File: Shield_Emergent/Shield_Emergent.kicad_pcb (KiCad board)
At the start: 2 copper layers, 33.4 x 63.5 mm, 23 parts, among them J1 Conn_01x02_Female, J2 Conn_01x04_Male, J3 Conn_01x02_Female, J4 Conn_01x04_Male, U1 Raspberri_Pi_Pico, U2 TPS2553, U3 TPS2553

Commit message: v1.3 Power of RPI_PICO and Shield was splitted
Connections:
- U1 pad 39: VBUS -> unconnected-(U1-Pad39)
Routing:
- net VBUS: track 36.0 -> 24.4 mm
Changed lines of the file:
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@@
   (net 36 "unconnected-(U1-Pad40)")
   (net 37 "+3V3")
+  (net 38 "unconnected-(U1-Pad39)")
   (footprint "MountingHole:MountingHole_2.7mm_M2.5" (layer "F.Cu")
     (at 46.54 81.96)
@@
       (net 2 "GND") (pinfunction "GND") (pintype "power_in"))
     (pad "39" thru_hole oval locked (at -21.59 -8.89 270) (size 1.6 4) (drill 1) (layers *.Cu *.Mask)
-      (net 1 "VBUS") (pinfunction "VSYS") (pintype "power_in"))
+      (net 38 "unconnected-(U1-Pad39)") (pinfunction "VSYS") (pintype "power_in"))
     (pad "40" thru_hole oval locked (at -24.13 -8.89 270) (size 1.6 4) (drill 1) (layers *.Cu *.Mask)
       (net 36 "unconnected-(U1-Pad40)") (pinfunction "VBUS") (pintype "power_in"))
@@
   (gr_rect (start 21.4 21.1) (end 54.8 84.6) (layer "Edge.Cuts") (width 0.1) (fill none))
   (segment (start 37.7 42.9) (end 37.4 42.9) (width 0.8) (layer "B.Cu") (net 1))
-  (segment (start 42.7 32.6) (end 44.14 31.16) (width 2) (layer "B.Cu") (net 1))
   (segment (start 32.7 46.1625) (end 32.6875 46.15) (width 0.5) (layer "B.Cu") (net 1))
   (segment (start 39.24 46.55) (end 39.4275 46.3625) (width 0.8) (layer "B.Cu") (net 1))
@@
   (segment (start 32.7 48) (end 32.7 46.1625) (width 0.7) (layer "B.Cu") (net 1))
   (segment (start 39.4275 46.3625) (end 39.4275 44.6275) (width 1) (layer "B.Cu") (net 1))
-  (segment (start 41.3 37.4) (end 42.7 36) (width 2) (layer "B.Cu") (net 1))
   (segment (start 39.4275 44.6275) (end 37.7 42.9) (width 1) (layer "B.Cu") (net 1))
   (segment (start 32.6875 46.15) (end 32.6875 44.8625) (width 1) (layer "B.Cu") (net 1))
-  (segment (start 42.7 36) (end 42.7 32.6) (width 2) (layer "B.Cu") (net 1))
-  (segment (start 39.6 37.4) (end 41.3 37.4) (width 2) (layer "B.Cu") (net 1))
   (segment (start 37.4 37.4) (end 37.4 42.9) (width 2) (layer "B.Cu") (net 1))
   (segment (start 39.4275 46.3625) (end 39.365 46.3) (width 0.8) (layer "B.Cu") (net 1))
@@
   (segment (start 39.24 48.2125) (end 39.24 46.55) (width 0.8) (layer "B.Cu") (net 1))
   (segment (start 32.6875 44.8625) (end 34.65 42.9) (width 1) (layer "B.Cu") (net 1))
-  (segment (start 44.14 31.16) (end 46.54 31.16) (width 2) (layer "B.Cu") (net 1))
   (segment (start 37.4 37.4) (end 39.6 37.4) (width 2) (layer "B.Cu") (net 1))
   (via (at 34.35 39.95) (size 0.8) (drill 0.4) (layers "F.Cu" "B.Cu") (free) (net 2))

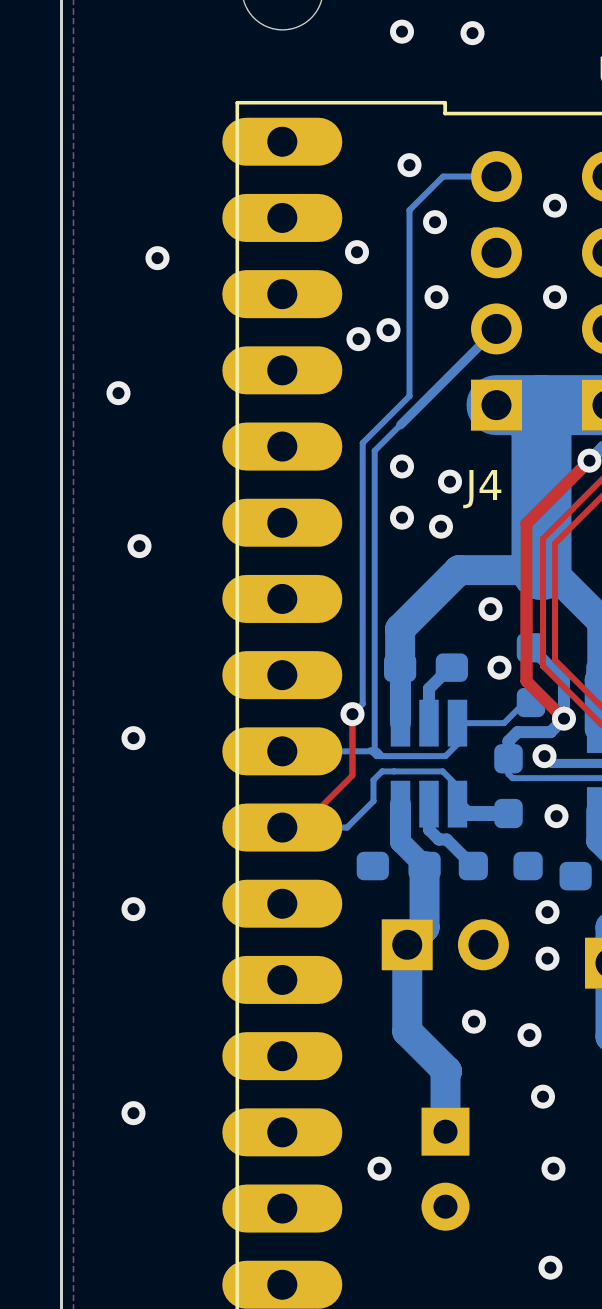
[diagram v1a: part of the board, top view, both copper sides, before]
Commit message: v1.4 four Buttons protos were added
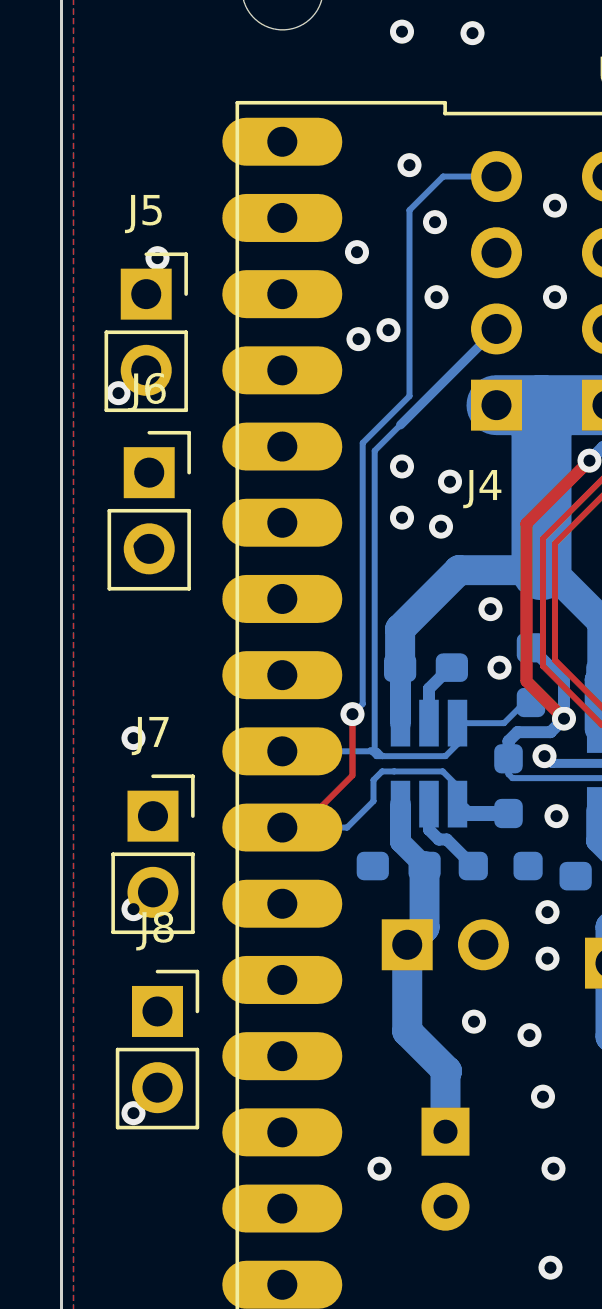
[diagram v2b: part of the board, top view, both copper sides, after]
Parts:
- added J5: Conn_01x02_Female, Connector_PinSocket_2.54mm:PinSocket_1x02_P2.54mm_Vertical, F.Cu at (24.2, 33.7)
- added J6: Conn_01x02_Female, Connector_PinSocket_2.54mm:PinSocket_1x02_P2.54mm_Vertical, F.Cu at (24.3, 39.6)
- added J7: Conn_01x02_Female, Connector_PinSocket_2.54mm:PinSocket_1x02_P2.54mm_Vertical, F.Cu at (24.4, 51.1)
- added J8: Conn_01x02_Female, Connector_PinSocket_2.54mm:PinSocket_1x02_P2.54mm_Vertical, F.Cu at (24.6, 57.6)
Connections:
- U1 pad 11: unconnected-(U1-Pad11) -> Net-(U1-Pad11)
- U1 pad 12: unconnected-(U1-Pad12) -> Net-(U1-Pad12)
- U1 pad 4: unconnected-(U1-Pad4) -> Net-(U1-Pad4)
- U1 pad 5: unconnected-(U1-Pad5) -> Net-(U1-Pad5)

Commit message: v1.5 Buttons Polarity was changed
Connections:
- J5 pad 1: GND -> Net-(U1-Pad4)
- J5 pad 2: Net-(U1-Pad4) -> GND
- J6 pad 1: GND -> Net-(J6-Pad1)
- J6 pad 2: Net-(U1-Pad5) -> GND
- J7 pad 1: GND -> Net-(J7-Pad1)
- J7 pad 2: Net-(U1-Pad11) -> GND
- J8 pad 1: GND -> Net-(U1-Pad12)
- J8 pad 2: Net-(U1-Pad12) -> GND
- U1 pad 11: Net-(U1-Pad11) -> Net-(J7-Pad1)
- U1 pad 5: Net-(U1-Pad5) -> Net-(J6-Pad1)
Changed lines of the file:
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@@
   (net 12 "unconnected-(U1-Pad2)")
   (net 13 "Net-(U1-Pad4)")
-  (net 14 "Net-(U1-Pad5)")
+  (net 14 "Net-(J7-Pad1)")
   (net 15 "unconnected-(U1-Pad6)")
   (net 16 "unconnected-(U1-Pad7)")
-  (net 17 "Net-(U1-Pad11)")
+  (net 17 "Net-(J6-Pad1)")
   (net 18 "Net-(U1-Pad12)")
   (net 19 "unconnected-(U1-Pad14)")
@@
     (fp_line (start 1.27 -0.635) (end 1.27 3.81) (layer "F.Fab") (width 0.1))
     (pad "1" thru_hole rect (at 0 0) (size 1.7 1.7) (drill 1) (layers *.Cu *.Mask)
-      (net 2 "GND") (pinfunction "Pin_1") (pintype "passive"))
+      (net 18 "Net-(U1-Pad12)") (pinfunction "Pin_1") (pintype "passive"))
     (pad "2" thru_hole oval (at 0 2.54) (size 1.7 1.7) (drill 1) (layers *.Cu *.Mask)
-      (net 18 "Net-(U1-Pad12)") (pinfunction "Pin_2") (pintype "passive"))
+      (net 2 "GND") (pinfunction "Pin_2") (pintype "passive"))
     (model "${KICAD6_3DMODEL_DIR}/Connector_PinSocket_2.54mm.3dshapes/PinSocket_1x02_P2.54mm_Vertical.wrl"
       (offset (xyz 0 0 0))
@@
       (net 13 "Net-(U1-Pad4)") (pinfunction "GP2") (pintype "bidirectional"))
     (pad "5" thru_hole oval locked (at -13.97 8.89 270) (size 1.6 4) (drill 1) (layers *.Cu *.Mask)
-      (net 14 "Net-(U1-Pad5)") (pinfunction "GP3") (pintype "bidirectional"))
+      (net 17 "Net-(J6-Pad1)") (pinfunction "GP3") (pintype "bidirectional"))
     (pad "6" thru_hole oval locked (at -11.43 8.89 270) (size 1.6 4) (drill 1) (layers *.Cu *.Mask)
       (net 15 "unconnected-(U1-Pad6)") (pinfunction "GP4/SDA") (pintype "bidirectional"))
@@
       (net 8 "FLT2") (pinfunction "GP7") (pintype "bidirectional"))
     (pad "11" thru_hole oval locked (at 1.27 8.89 270) (size 1.6 4) (drill 1) (layers *.Cu *.Mask)
-      (net 17 "Net-(U1-Pad11)") (pinfunction "GP8") (pintype "bidirectional"))
+      (net 14 "Net-(J7-Pad1)") (pinfunction "GP8") (pintype "bidirectional"))
     (pad "12" thru_hole oval locked (at 3.81 8.89 270) (size 1.6 4) (drill 1) (layers *.Cu *.Mask)
       (net 18 "Net-(U1-Pad12)") (pinfunction "GP9") (pintype "bidirectional"))
@@
     (fp_line (start -1.27 -1.27) (end 0.635 -1.27) (layer "F.Fab") (width 0.1))
     (pad "1" thru_hole rect (at 0 0) (size 1.7 1.7) (drill 1) (layers *.Cu *.Mask)
-      (net 2 "GND") (pinfunction "Pin_1") (pintype "passive"))
+      (net 14 "Net-(J7-Pad1)") (pinfunction "Pin_1") (pintype "passive"))
     (pad "2" thru_hole oval (at 0 2.54) (size 1.7 1.7) (drill 1) (layers *.Cu *.Mask)
-      (net 17 "Net-(U1-Pad11)") (pinfunction "Pin_2") (pintype "passive"))
+      (net 2 "GND") (pinfunction "Pin_2") (pintype "passive"))
     (model "${KICAD6_3DMODEL_DIR}/Connector_PinSocket_2.54mm.3dshapes/PinSocket_1x02_P2.54mm_Vertical.wrl"
       (offset (xyz 0 0 0))
@@
     (fp_line (start 1.27 3.81) (end -1.27 3.81) (layer "F.Fab") (width 0.1))
     (pad "1" thru_hole rect (at 0 0) (size 1.7 1.7) (drill 1) (layers *.Cu *.Mask)
-      (net 2 "GND") (pinfunction "Pin_1") (pintype "passive"))
+      (net 13 "Net-(U1-Pad4)") (pinfunction "Pin_1") (pintype "passive"))
     (pad "2" thru_hole oval (at 0 2.54) (size 1.7 1.7) (drill 1) (layers *.Cu *.Mask)
-      (net 13 "Net-(U1-Pad4)") (pinfunction "Pin_2") (pintype "passive"))
+      (net 2 "GND") (pinfunction "Pin_2") (pintype "passive"))
     (model "${KICAD6_3DMODEL_DIR}/Connector_PinSocket_2.54mm.3dshapes/PinSocket_1x02_P2.54mm_Vertical.wrl"
       (offset (xyz 0 0 0))
@@
     (fp_line (start -1.27 3.81) (end -1.27 -1.27) (layer "F.Fab") (width 0.1))
     (pad "1" thru_hole rect (at 0 0) (size 1.7 1.7) (drill 1) (layers *.Cu *.Mask)
-      (net 2 "GND") (pinfunction "Pin_1") (pintype "passive"))
+      (net 17 "Net-(J6-Pad1)") (pinfunction "Pin_1") (pintype "passive"))
     (pad "2" thru_hole oval (at 0 2.54) (size 1.7 1.7) (drill 1) (layers *.Cu *.Mask)
-      (net 14 "Net-(U1-Pad5)") (pinfunction "Pin_2") (pintype "passive"))
+      (net 2 "GND") (pinfunction "Pin_2") (pintype "passive"))
     (model "${KICAD6_3DMODEL_DIR}/Connector_PinSocket_2.54mm.3dshapes/PinSocket_1x02_P2.54mm_Vertical.wrl"
       (offset (xyz 0 0 0))

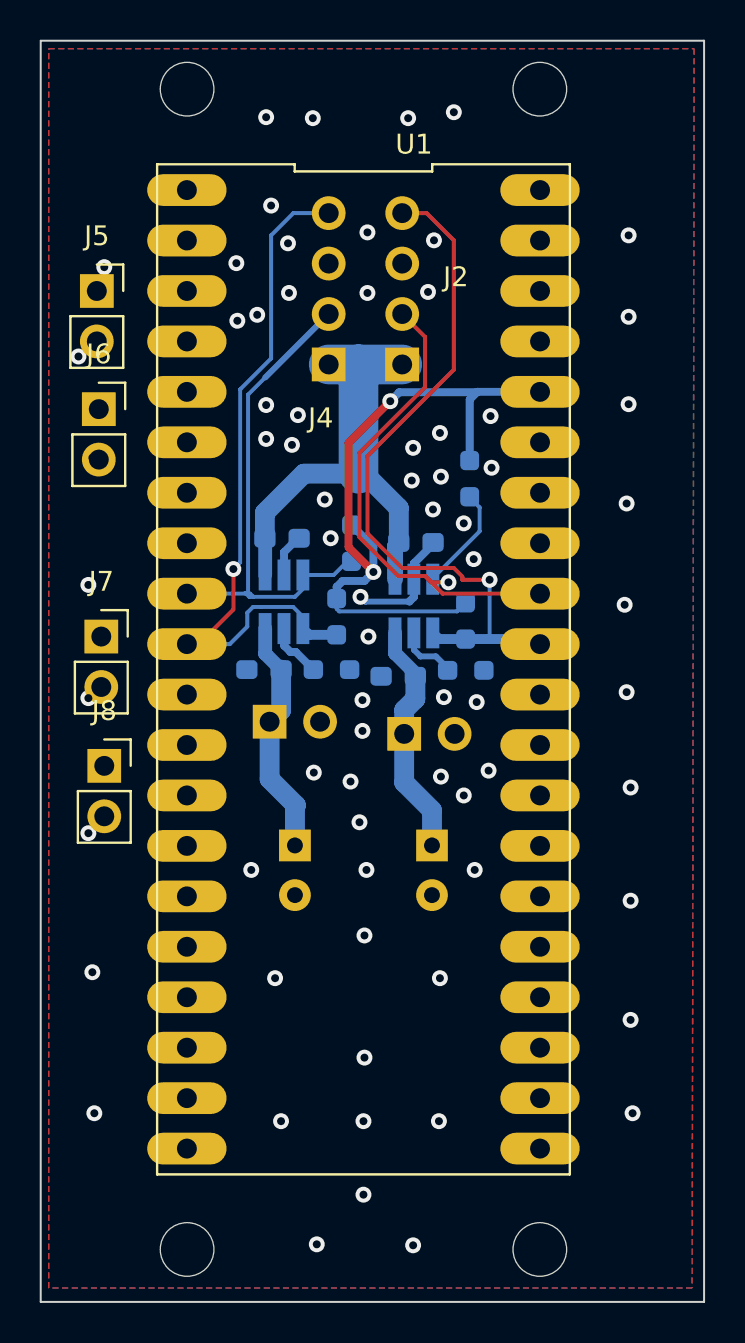
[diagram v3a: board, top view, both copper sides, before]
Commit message: v1.6 single connector for all purposes was added
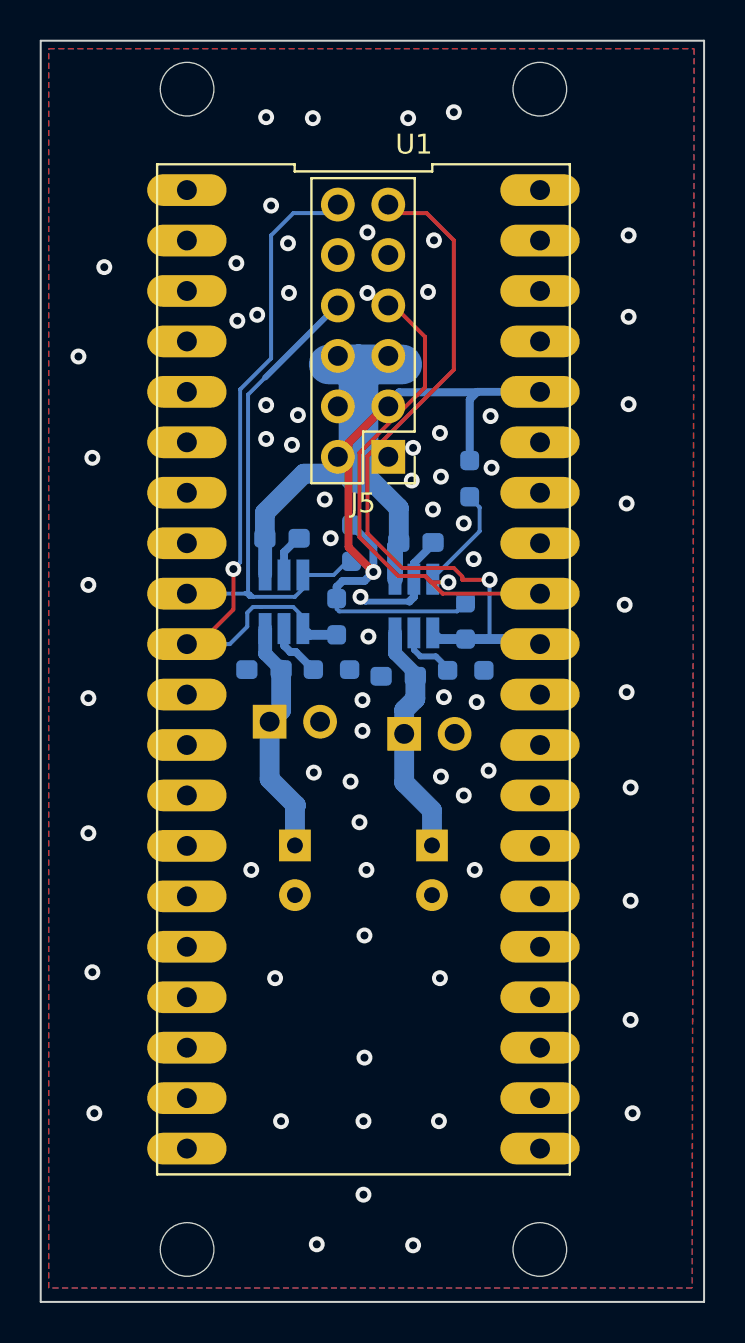
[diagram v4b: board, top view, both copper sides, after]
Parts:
- removed J2, J4: Conn_01x04_Male, Connector_PinSocket_2.54mm:PinSocket_1x04_P2.54mm_Vertical
- removed J6, J7, J8: Conn_01x02_Female, Connector_PinSocket_2.54mm:PinSocket_1x02_P2.54mm_Vertical
- J5: value Conn_01x02_Female -> Conn_02x06_Odd_Even; footprint Connector_PinSocket_2.54mm:PinSocket_1x02_P2.54mm_Vertical -> Connector_PinHeader_2.54mm:PinHeader_2x06_P2.54mm_Vertical
- moved J5 16.9 mm to (38.9, 42.0), turned to 180 degrees
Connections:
- J5 pad 1: Net-(U1-Pad4) -> VBUS
- J5 pad 2: GND -> VBUS
- U1 pad 11: Net-(J7-Pad1) -> B2
- U1 pad 12: Net-(U1-Pad12) -> B4
- U1 pad 4: Net-(U1-Pad4) -> B1
- U1 pad 5: Net-(J6-Pad1) -> B3

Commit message: v1.7 DRC was conducted
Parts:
- moved R1 2.98 mm to (42.1, 40.3), turned to 180 degrees
- moved J5 0.80 mm to (38.9, 42.9)
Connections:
- J5 pad 10: B2 -> B3
- J5 pad 11: B3 -> B2
- J5 pad 12: B4 -> B1
- J5 pad 9: B1 -> B4
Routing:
- net B4: track 0.00 -> 30.2 mm
- net B2: track 0.00 -> 30.1 mm
- net EN1: track 30.4 -> 16.8 mm
- net B1: track 0.00 -> 11.5 mm
- net B3: track 0.00 -> 11.3 mm
- net FLT1: track 35.6 -> 25.3 mm, vias 1 -> 0
- net VBUS: track 24.4 -> 16.0 mm
- net FLT2: track 36.4 -> 30.6 mm
- net +3V3: track 34.3 -> 29.3 mm
- net EN2: track 26.4 -> 21.9 mm
- net GND: vias 72 -> 98
